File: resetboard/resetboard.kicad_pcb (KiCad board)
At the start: 2 copper layers, 85 x 20 mm, 24 parts, among them J1 USB_C_Receptacle_USB2.0, J2 Conn_02x20_Odd_Even, J3 Conn_01x02, J4 Conn_01x06, SW1 SW_SPST, U1 PCF8523TK, U2 SE050, Y1 Crystal_Small

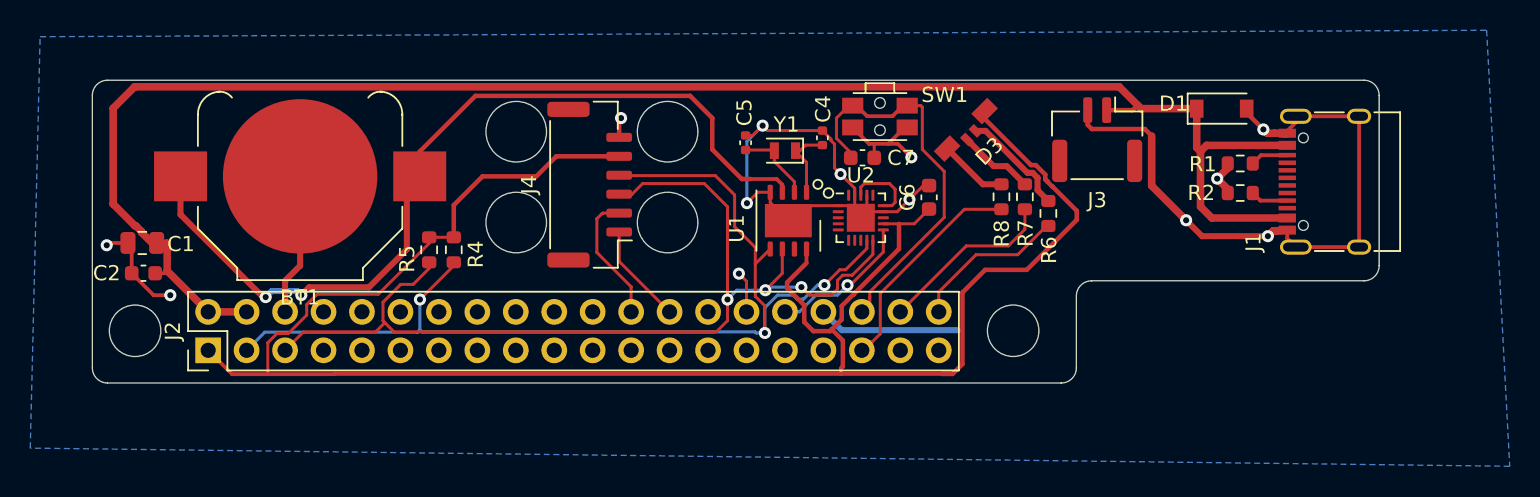
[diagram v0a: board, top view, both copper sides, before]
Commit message: Remove ziptie holes Add filtering to RTC supply Add NFET-controlled fan on GPIO18 Switch fan connector to horizontal Rearrange parts to move fan connector to left edge of board Rotate LED towards edge Relabel R and B channels of RGB LED to match part Add vendor STEP model for RGB LED Regenerate STEP file
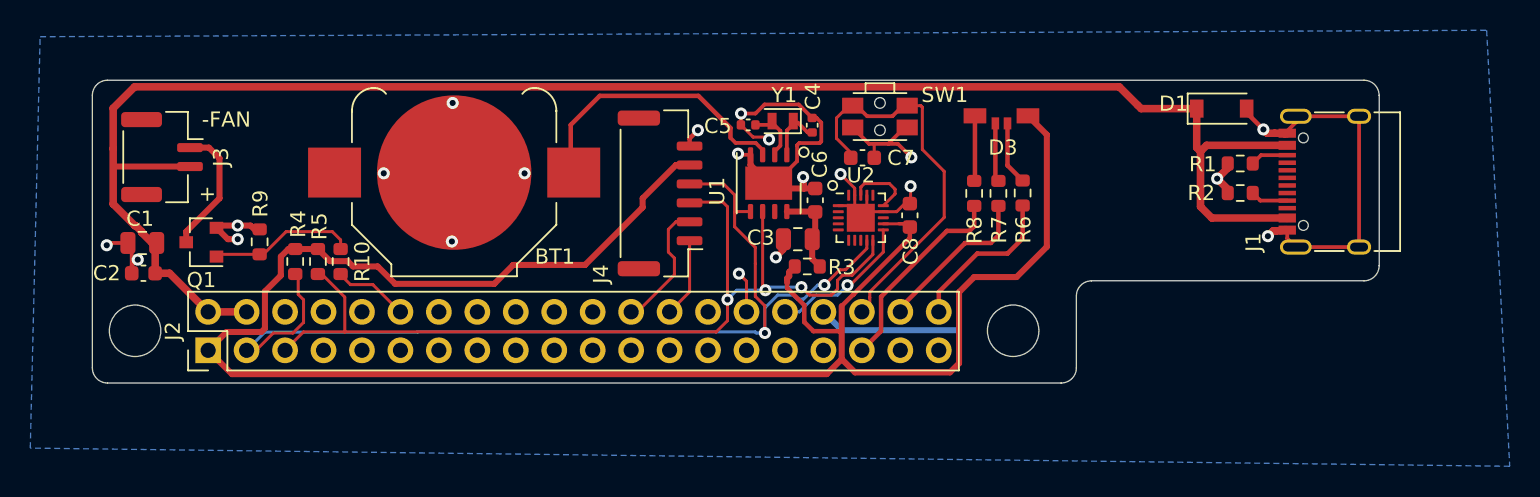
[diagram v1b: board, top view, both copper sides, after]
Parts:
- added C3: 10u, Capacitor_SMD:C_0805_2012Metric, F.Cu at (193.8, 104.8)
- added C8: 100n, Capacitor_SMD:C_0603_1608Metric, F.Cu at (201.2, 103.2)
- added Q1: 2N7002, Package_TO_SOT_SMD:SOT-23, F.Cu at (154.4, 105.0)
- added R10: 33R, Resistor_SMD:R_0603_1608Metric, F.Cu at (163.7, 106.2)
- added R3: 33R, Resistor_SMD:R_0603_1608Metric, F.Cu at (194.5, 106.5)
- added R9: 5.1k, Resistor_SMD:R_0603_1608Metric, F.Cu at (158.3, 104.9)
- D3: value LED_ABGR -> EASV3015RGBA0
- J3: footprint Connector_JST:JST_GH_BM02B-GHS-TBT_1x02-1MP_P1.25mm_Vertical -> Connector_JST:JST_GH_SM02B-GHS-TB_1x02-1MP_P1.25mm_Horizontal
- moved J3 61.8 mm to (151.8, 99.3), turned to 270 degrees
- moved R4 10.5 mm to (160.7, 106.2)
- moved BT1 10.2 mm to (171.2, 100.3)
- moved C6 7.52 mm to (195.0, 102.2)
- moved R5 7.39 mm to (162.2, 106.2)
- moved J4 4.69 mm to (184.8, 101.7)
- moved U1 2.80 mm to (191.9, 101.0)
- moved D3 2.53 mm to (207.3, 96.6), turned to 90 degrees
- moved R6 2.17 mm to (208.7, 101.7)
- moved Y1 1.96 mm to (192.8, 97.0)
- moved R8 1.81 mm to (205.5, 101.7)
- moved R7 1.76 mm to (207.1, 101.7)
- moved C5 1.19 mm to (190.6, 97.2), turned to 180 degrees
- moved C4 1.07 mm to (194.8, 97.2)
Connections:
- C6 pad 1: VDD -> Net-(C3-Pad1)
- J2 pad 12: Net-(J2-Pad12) -> /FAN
- J2 pad 35: /B -> /R
- J2 pad 40: /R -> /B
- J3 pad 1: /5VIN -> Net-(J3-Pad1)
- J3 pad 2: GND -> /5VIN
- R6 pad 2: /R -> /B
- R8 pad 2: /B -> /R
- U1 pad 8: VDD -> Net-(C3-Pad1)
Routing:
- net Net-(BT1-Pad1): track 57.9 -> 18.9 mm, vias 2 -> 0
- net GND: track 115.8 -> 93.9 mm, vias 13 -> 21
- net Net-(Q1-Pad1): track 0.00 -> 9.71 mm
- net Net-(J3-Pad1): track 0.00 -> 8.70 mm
- net Net-(C3-Pad1): track 0.00 -> 5.78 mm
- net /SCL: track 67.7 -> 62.5 mm
- net /FAN: track 0.00 -> 5.01 mm
- net /B: track 14.6 -> 10.5 mm
- net /R: track 10.4 -> 13.5 mm
- net /SDA: track 70.9 -> 67.8 mm, vias 3 -> 2
- net Net-(D3-Pad4): track 7.21 -> 4.19 mm
- net VDD: track 130.7 -> 133.6 mm
- net /5VIN: track 114.3 -> 117.1 mm
- net Net-(C5-Pad1): track 5.22 -> 3.67 mm
- net Net-(J2-Pad26): track 6.65 -> 5.25 mm
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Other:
- outline, holes or cut-outs redrawn
- board text added: "+"
- board text added: "-FAN"
